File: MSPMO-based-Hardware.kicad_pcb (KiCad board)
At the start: 2 copper layers, 12 parts, among them J1 USB_C_Receptacle_USB2.0_14P, U1 MSPMOG3507SPTR, X1 8MHz

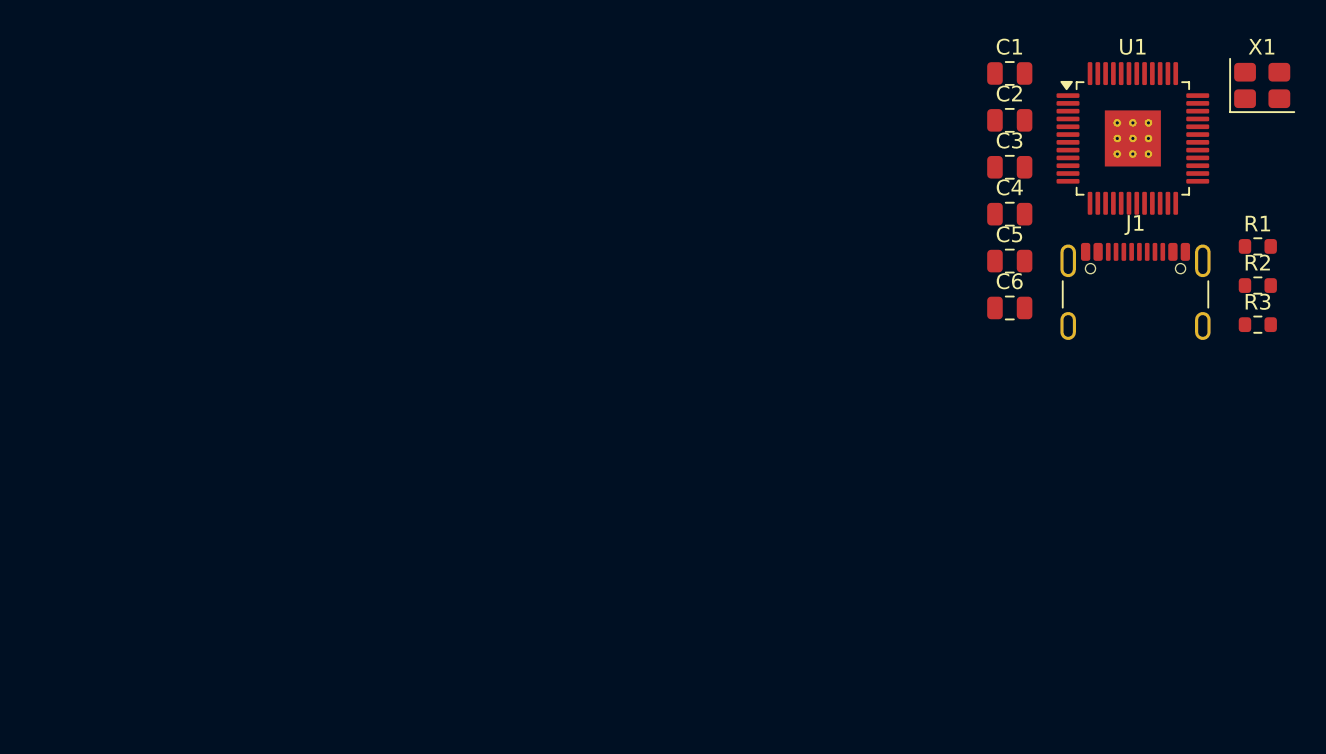
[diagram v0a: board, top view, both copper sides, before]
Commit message: featardware): major(h PCB redesign with USB-C, SWD programming, and sensor integration
Redesigned MSPM0-based hardware PCB with significant changes:
- Added USB-C receptacle with ESD protection (USBLC6-2SC6)
- Added Tag-Connect TC2030 SWD programming header
- Added LIS2DH 3-axis accelerometer with I2C interface
- Added CH340E USB-to-serial converter for UART debugging
- Added SPX3819 LDO voltage regulator (3.3V output)
- Relocated microcontroller and reorganized component placement
- Added full PCB stackup configuration with FR4 dielectric specs
- Added mounting holes and fiducial markers for manufacturing
- Updated net connectivity (connected previously unconnected pins)
- Added silkscreen branding

This is a comprehensive hardware revision with new peripherals and interfaces.
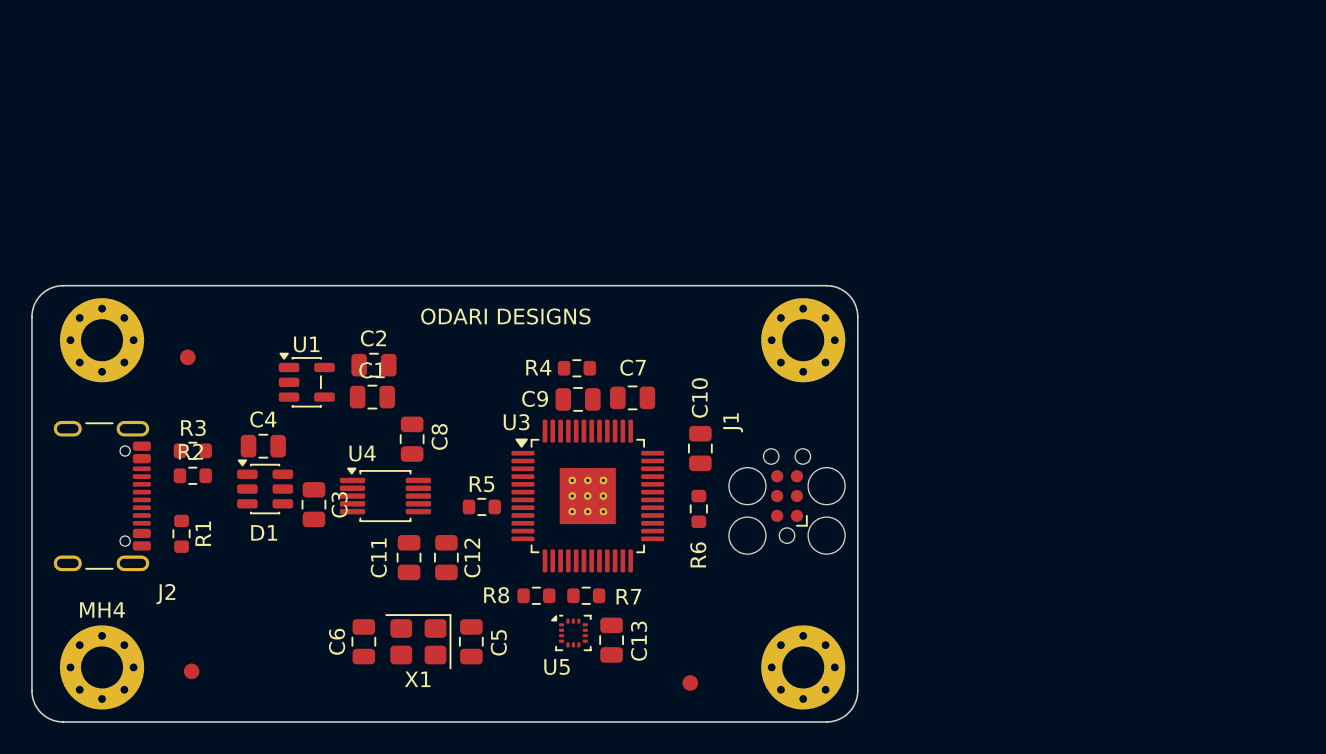
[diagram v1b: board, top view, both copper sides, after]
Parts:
- added C10: 470n, Capacitor_SMD:C_0805_2012Metric, F.Cu at (95.4, 96.0)
- added C11: 470n, Capacitor_SMD:C_0805_2012Metric, F.Cu at (76.7, 103.0)
- added C12: 470n, Capacitor_SMD:C_0805_2012Metric, F.Cu at (79.1, 103.0)
- added C13: 470n, Capacitor_SMD:C_0805_2012Metric, F.Cu at (89.7, 108.2)
- added C7: 470n, Capacitor_SMD:C_0805_2012Metric, F.Cu at (91.0, 92.7)
- added C8: 10u, Capacitor_SMD:C_0805_2012Metric, F.Cu at (76.9, 95.3)
- added C9: 470n, Capacitor_SMD:C_0805_2012Metric, F.Cu at (87.5, 92.8)
- added D1: USBLC6-2SC6, Package_TO_SOT_SMD:SOT-23-6, F.Cu at (67.5, 98.5)
- added FID1: Fiducial, Fiducial:Fiducial_1mm_Mask2mm, F.Cu at (62.8, 110.2)
- added FID2: Fiducial, Fiducial:Fiducial_1mm_Mask2mm, F.Cu at (62.5, 90.1)
- added FID3: Fiducial, Fiducial:Fiducial_1mm_Mask2mm, F.Cu at (94.8, 111.0)
- added J2: USB_C_Receptacle_USB2.0_16P, Connector_USB:USB_C_Receptacle_GCT_USB4105-xx-A_16P_TopMnt_Horizontal, F.Cu at (55.9, 99.0)
- added MH1: M3, MountingHole:MountingHole_2.7mm_M2.5_Pad_Via, F.Cu at (57.0, 89.0)
- added MH2: M3, MountingHole:MountingHole_2.7mm_M2.5_Pad_Via, F.Cu at (102.0, 89.0)
- added MH3: M3, MountingHole:MountingHole_2.7mm_M2.5_Pad_Via, F.Cu at (102.0, 110.0)
- added MH4: M3, MountingHole:MountingHole_2.7mm_M2.5_Pad_Via, F.Cu at (57.0, 110.0)
- added R4: 0R, Resistor_SMD:R_0603_1608Metric, F.Cu at (87.5, 90.8)
- added R5: 100K, Resistor_SMD:R_0603_1608Metric, F.Cu at (81.4, 99.7)
- added R6: 5k1, Resistor_SMD:R_0603_1608Metric, F.Cu at (95.3, 99.8)
- added R7: 5k1, Resistor_SMD:R_0603_1608Metric, F.Cu at (88.1, 105.4)
- added R8: 5k1, Resistor_SMD:R_0603_1608Metric, F.Cu at (84.9, 105.4)
- added U3: MSPMOG3507SPTR, Package_QFP:LQFP-48-1EP_7x7mm_P0.5mm_EP3.6x3.6mm_ThermalVias, F.Cu at (88.2, 99.0)
- added U4: CH340E, Package_SO:MSOP-10_3x3mm_P0.5mm, F.Cu at (75.2, 99.0)
- added U5: LIS2DH, Package_LGA:LGA-14_2x2mm_P0.35mm_LayoutBorder3x4y, F.Cu at (87.2, 107.8)
- J1: value USB_C_Receptacle_USB2.0_14P -> Conn_ARM_SWD_TagConnect_TC2030; footprint Connector_USB:USB_C_Receptacle_GCT_USB4105-xx-A_16P_TopMnt_Horizontal -> Connector:Tag-Connect_TC2030-IDC-FP_2x03_P1.27mm_Vertical
- R1: value 0R -> 5k1
- R3: value 100K -> 0R
- U1: value MSPMOG3507SPTR -> SPX3819M5-L-3-3; footprint Package_QFP:LQFP-48-1EP_7x7mm_P0.5mm_EP3.6x3.6mm_ThermalVias -> Package_TO_SOT_SMD:SOT-23-5
- moved R1 71.5 mm to (62.1, 101.4), turned to -90 degrees
- moved R2 69.4 mm to (62.8, 97.7)
- moved R3 68.8 mm to (62.8, 96.1)
- moved X1 64.9 mm to (77.3, 108.3), turned to 180 degrees
- moved U1 55.3 mm to (70.1, 91.7)
- moved C4 50.2 mm to (67.3, 95.8)
- moved C3 49.6 mm to (70.6, 99.5), turned to -90 degrees
- moved C6 46.7 mm to (73.8, 108.3), turned to 90 degrees
- moved C1 45.9 mm to (74.3, 92.7)
- moved C2 43.7 mm to (74.5, 90.6)
- moved C5 42.3 mm to (80.7, 108.3), turned to -90 degrees
- moved J1 25.4 mm to (101.0, 99.0), turned to 90 degrees
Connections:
- C1 pad 1: +1V35 -> Net-(U1-BP)
- C3 pad 1: /VREF- -> +VBUS
- C3 pad 2: /VREF+ -> GND
- C4 pad 1: /NRST -> +5V
- C5 pad 1: /HFXOUT -> /HFXIN
- C6 pad 1: /HFXIN -> /HFXOUT
- R1 pad 1: /VREF- -> /USBCD+
- R2 pad 1: +3.3V -> /USBCD-
- R2 pad 2: /NRST -> GND
- R3 pad 1: GND -> +VBUS
- R3 pad 2: /ROSC -> +5V
- U1 pad 1: unconnected-(U1-PA0/FCC_IN-Pad1) -> +5V
- U1 pad 2: unconnected-(U1-PA1-Pad2) -> GND
- U1 pad 3: unconnected-(U1-PA28-Pad3) -> +5V
- U1 pad 4: /NRST -> Net-(U1-BP)
- U1 pad 5: (no net) -> +3.3V
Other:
- board outline added: 53 x 28 mm
- rule pad_to_mask_clearance: 0 -> 0.1
- board text added: "ODARI DESIGNS"
